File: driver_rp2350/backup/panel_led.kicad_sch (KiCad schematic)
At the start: 342 parts

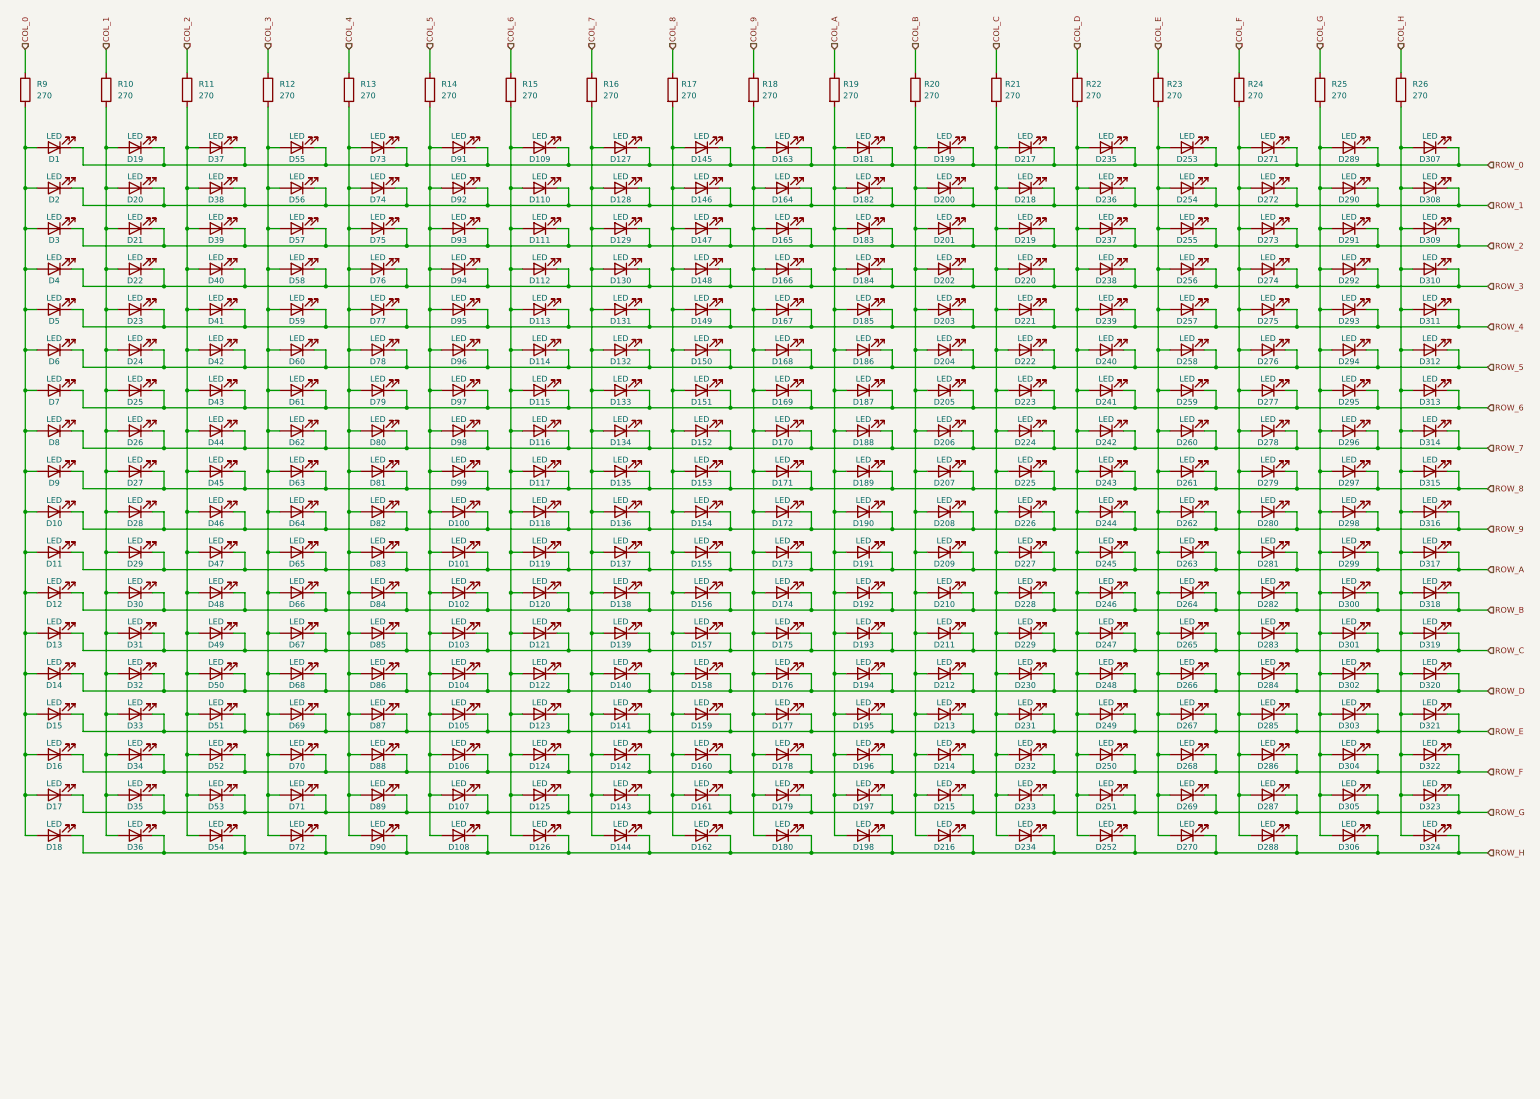
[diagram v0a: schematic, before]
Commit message: Renamed LED array due to kicad compatibility issues.
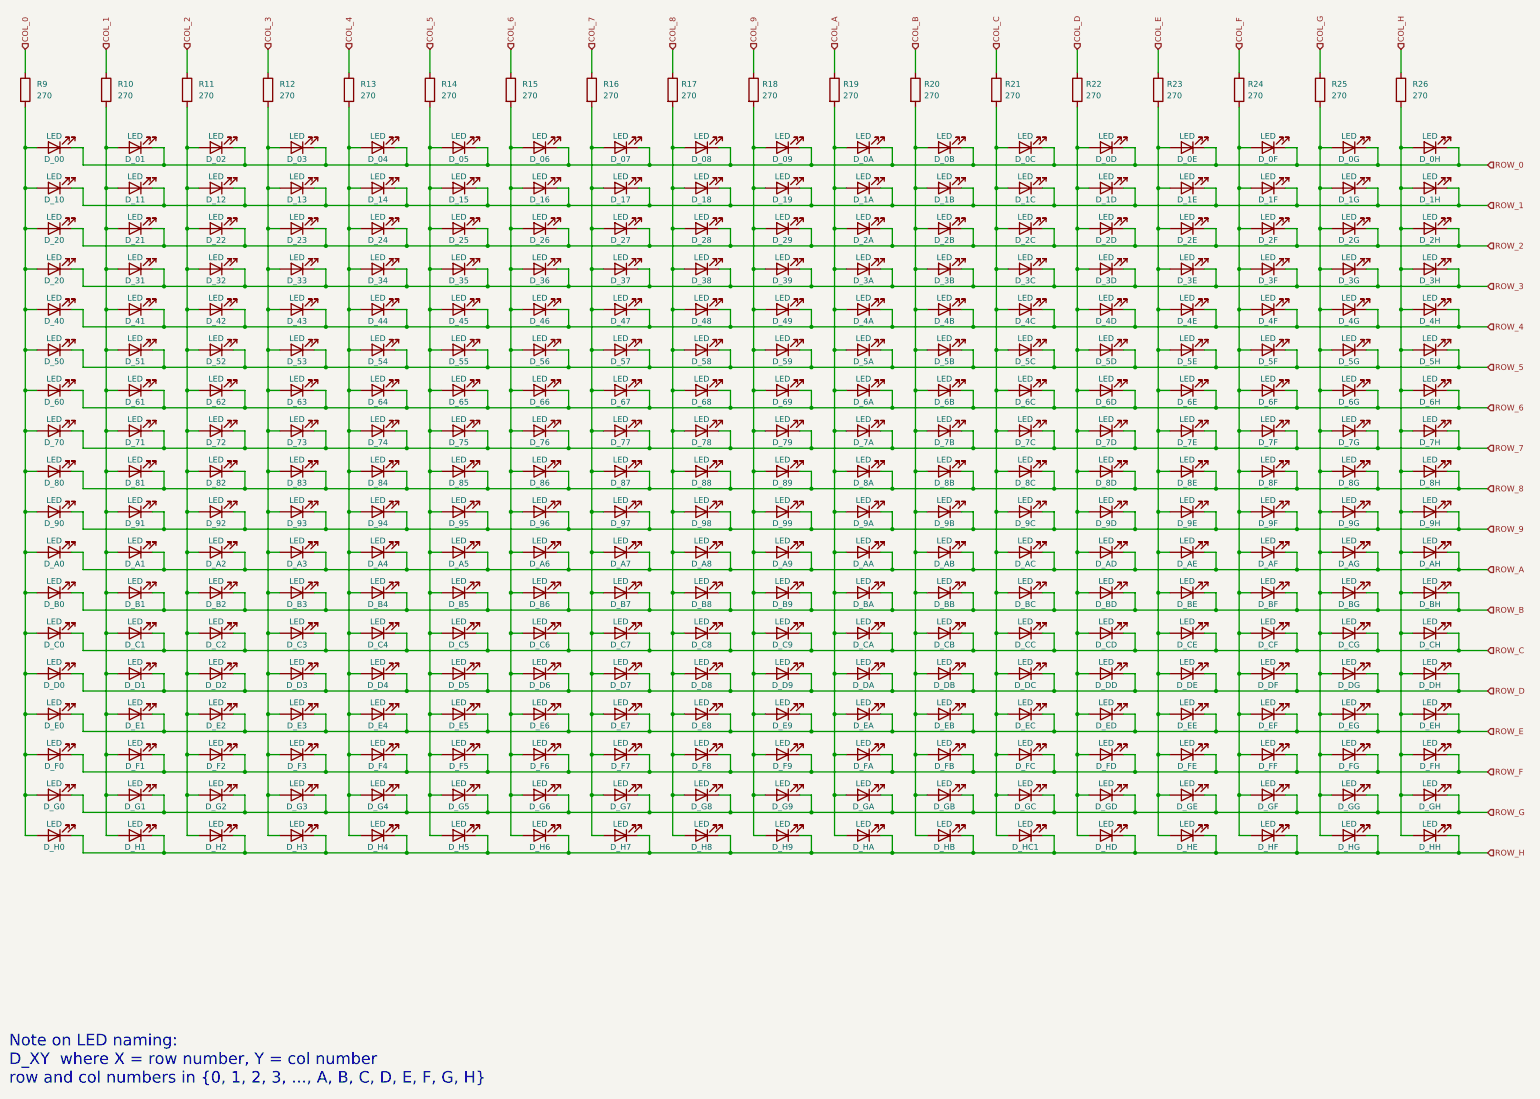
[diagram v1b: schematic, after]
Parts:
- removed D100, D101, D102, D103, D104, D105, D106, D107, D108, D109, D110, D111, D112, D113, D114, D115, D116, D117, D118, D119, D120, D121, D122, D123, D124, D125, D126, D127, D128, D129, D130, D131, D132, D133, D134, D135, D136, D137, D138, D139, D140, D141, D142, D143, D144, D145, D146, D147, D148, D149, D150, D151, D152, D153, D154, D155, D156, D157, D158, D159, D160, D161, D162, D163, D164, D165, D166, D167, D168, D169, D170, D171, D172, D173, D174, D175, D176, D177, D178, D179, D180, D181, D182, D183, D184, D185, D186, D187, D188, D189, D19, D190, D191, D192, D193, D194, D195, D196, D197, D198, D199, D20, D200, D201, D202, D203, D204, D205, D206, D207, D208, D209, D21, D210, D211, D212, D213, D214, D215, D216, D217, D218, D219, D22, D220, D221, D222, D223, D224, D225, D226, D227, D228, D229, D23, D230, D231, D232, D233, D234, D235, D236, D237, D238, D239, D24, D240, D241, D242, D243, D244, D245, D246, D247, D248, D249, D25, D250, D251, D252, D253, D254, D255, D256, D257, D258, D259, D26, D260, D261, D262, D263, D264, D265, D266, D267, D268, D269, D27, D270, D271, D272, D273, D274, D275, D276, D277, D278, D279, D28, D280, D281, D282, D283, D284, D285, D286, D287, D288, D289, D29, D290, D291, D292, D293, D294, D295, D296, D297, D298, D299, D30, D300, D301, D302, D303, D304, D305, D306, D307, D308, D309, D31, D310, D311, D312, D313, D314, D315, D316, D317, D318, D319, D32, D320, D321, D322, D323, D324, D33, D34, D35, D36, D37, D38, D39, D40, D41, D42, D43, D44, D45, D46, D47, D48, D49, D50, D51, D52, D53, D54, D55, D56, D57, D58, D59, D60, D61, D62, D63, D64, D65, D66, D67, D68, D69, D70, D71, D72, D73, D74, D75, D76, D77, D78, D79, D80, D81, D82, D83, D84, D85, D86, D87, D88, D89, D90, D91, D92, D93, D94, D95, D96, D97, D98, D99: LED, panel_custom:LED_0402_1005Metric, symbol Device:LED
- added D_01, D_02, D_03, D_04, D_05, D_06, D_07, D_08, D_09, D_0A, D_0B, D_0C, D_0D, D_0E, D_0F, D_0G, D_0H, D_11, D_12, D_13, D_14, D_15, D_16, D_17, D_18, D_19, D_1A, D_1B, D_1C, D_1D, D_1E, D_1F, D_1G, D_1H, D_21, D_22, D_23, D_24, D_25, D_26, D_27, D_28, D_29, D_2A, D_2B, D_2C, D_2D, D_2E, D_2F, D_2G, D_2H, D_31, D_32, D_33, D_34, D_35, D_36, D_37, D_38, D_39, D_3A, D_3B, D_3C, D_3D, D_3E, D_3F, D_3G, D_3H, D_41, D_42, D_43, D_44, D_45, D_46, D_47, D_48, D_49, D_4A, D_4B, D_4C, D_4D, D_4E, D_4F, D_4G, D_4H, D_51, D_52, D_53, D_54, D_55, D_56, D_57, D_58, D_59, D_5A, D_5B, D_5C, D_5D, D_5E, D_5F, D_5G, D_5H, D_61, D_62, D_63, D_64, D_65, D_66, D_67, D_68, D_69, D_6A, D_6B, D_6C, D_6D, D_6E, D_6F, D_6G, D_6H, D_71, D_72, D_73, D_74, D_75, D_76, D_77, D_78, D_79, D_7A, D_7B, D_7C, D_7D, D_7E, D_7F, D_7G, D_7H, D_81, D_82, D_83, D_84, D_85, D_86, D_87, D_88, D_89, D_8A, D_8B, D_8C, D_8D, D_8E, D_8F, D_8G, D_8H, D_91, D_92, D_93, D_94, D_95, D_96, D_97, D_98, D_99, D_9A, D_9B, D_9C, D_9D, D_9E, D_9F, D_9G, D_9H, D_A1, D_A2, D_A3, D_A4, D_A5, D_A6, D_A7, D_A8, D_A9, D_AA, D_AB, D_AC, D_AD, D_AE, D_AF, D_AG, D_AH, D_B1, D_B2, D_B3, D_B4, D_B5, D_B6, D_B7, D_B8, D_B9, D_BA, D_BB, D_BC, D_BD, D_BE, D_BF, D_BG, D_BH, D_C1, D_C2, D_C3, D_C4, D_C5, D_C6, D_C7, D_C8, D_C9, D_CA, D_CB, D_CC, D_CD, D_CE, D_CF, D_CG, D_CH, D_D1, D_D2, D_D3, D_D4, D_D5, D_D6, D_D7, D_D8, D_D9, D_DA, D_DB, D_DC, D_DD, D_DE, D_DF, D_DG, D_DH, D_E1, D_E2, D_E3, D_E4, D_E5, D_E6, D_E7, D_E8, D_E9, D_EA, D_EB, D_EC, D_ED, D_EE, D_EF, D_EG, D_EH, D_F1, D_F2, D_F3, D_F4, D_F5, D_F6, D_F7, D_F8, D_F9, D_FA, D_FB, D_FC, D_FD, D_FE, D_FF, D_FG, D_FH, D_G1, D_G2, D_G3, D_G4, D_G5, D_G6, D_G7, D_G8, D_G9, D_GA, D_GB, D_GC, D_GD, D_GE, D_GF, D_GG, D_GH, D_H1, D_H2, D_H3, D_H4, D_H5, D_H6, D_H7, D_H8, D_H9, D_HA, D_HB, D_HC1, D_HD, D_HE, D_HF, D_HG, D_HH: LED, panel_custom:LED_0402_1005Metric, symbol Device:LED
- renumbered D1 to D_00, D2 to D_10, D4 to D_20, D3 to D_20, D5 to D_40, D6 to D_50, D7 to D_60, D8 to D_70, D9 to D_80, D10 to D_90, D11 to D_A0, D12 to D_B0, D13 to D_C0, D14 to D_D0, D15 to D_E0, D16 to D_F0, D17 to D_G0, D18 to D_H0
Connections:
- net ROW_0: now also D_01.1 (K), D_02.1 (K), D_03.1 (K), D_04.1 (K), D_05.1 (K), D_06.1 (K), D_07.1 (K), D_08.1 (K), D_09.1 (K), D_0A.1 (K), D_0B.1 (K), D_0C.1 (K), D_0D.1 (K), D_0E.1 (K), D_0F.1 (K), D_0G.1 (K), D_0H.1 (K)
- net ROW_1: now also D_11.1 (K), D_12.1 (K), D_13.1 (K), D_14.1 (K), D_15.1 (K), D_16.1 (K), D_17.1 (K), D_18.1 (K), D_19.1 (K), D_1A.1 (K), D_1B.1 (K), D_1C.1 (K), D_1D.1 (K), D_1E.1 (K), D_1F.1 (K), D_1G.1 (K), D_1H.1 (K)
- net ROW_2: now also D_21.1 (K), D_22.1 (K), D_23.1 (K), D_24.1 (K), D_25.1 (K), D_26.1 (K), D_27.1 (K), D_28.1 (K), D_29.1 (K), D_2A.1 (K), D_2B.1 (K), D_2C.1 (K), D_2D.1 (K), D_2E.1 (K), D_2F.1 (K), D_2G.1 (K), D_2H.1 (K)
- net ROW_3: now also D_31.1 (K), D_32.1 (K), D_33.1 (K), D_34.1 (K), D_35.1 (K), D_36.1 (K), D_37.1 (K), D_38.1 (K), D_39.1 (K), D_3A.1 (K), D_3B.1 (K), D_3C.1 (K), D_3D.1 (K), D_3E.1 (K), D_3F.1 (K), D_3G.1 (K), D_3H.1 (K)
- net ROW_4: now also D_41.1 (K), D_42.1 (K), D_43.1 (K), D_44.1 (K), D_45.1 (K), D_46.1 (K), D_47.1 (K), D_48.1 (K), D_49.1 (K), D_4A.1 (K), D_4B.1 (K), D_4C.1 (K), D_4D.1 (K), D_4E.1 (K), D_4F.1 (K), D_4G.1 (K), D_4H.1 (K)
- net ROW_5: now also D_51.1 (K), D_52.1 (K), D_53.1 (K), D_54.1 (K), D_55.1 (K), D_56.1 (K), D_57.1 (K), D_58.1 (K), D_59.1 (K), D_5A.1 (K), D_5B.1 (K), D_5C.1 (K), D_5D.1 (K), D_5E.1 (K), D_5F.1 (K), D_5G.1 (K), D_5H.1 (K)
- net ROW_6: now also D_61.1 (K), D_62.1 (K), D_63.1 (K), D_64.1 (K), D_65.1 (K), D_66.1 (K), D_67.1 (K), D_68.1 (K), D_69.1 (K), D_6A.1 (K), D_6B.1 (K), D_6C.1 (K), D_6D.1 (K), D_6E.1 (K), D_6F.1 (K), D_6G.1 (K), D_6H.1 (K)
- net ROW_7: now also D_71.1 (K), D_72.1 (K), D_73.1 (K), D_74.1 (K), D_75.1 (K), D_76.1 (K), D_77.1 (K), D_78.1 (K), D_79.1 (K), D_7A.1 (K), D_7B.1 (K), D_7C.1 (K), D_7D.1 (K), D_7E.1 (K), D_7F.1 (K), D_7G.1 (K), D_7H.1 (K)
- net ROW_8: now also D_81.1 (K), D_82.1 (K), D_83.1 (K), D_84.1 (K), D_85.1 (K), D_86.1 (K), D_87.1 (K), D_88.1 (K), D_89.1 (K), D_8A.1 (K), D_8B.1 (K), D_8C.1 (K), D_8D.1 (K), D_8E.1 (K), D_8F.1 (K), D_8G.1 (K), D_8H.1 (K)
- net ROW_9: now also D_91.1 (K), D_92.1 (K), D_93.1 (K), D_94.1 (K), D_95.1 (K), D_96.1 (K), D_97.1 (K), D_98.1 (K), D_99.1 (K), D_9A.1 (K), D_9B.1 (K), D_9C.1 (K), D_9D.1 (K), D_9E.1 (K), D_9F.1 (K), D_9G.1 (K), D_9H.1 (K)
- net ROW_A: now also D_A1.1 (K), D_A2.1 (K), D_A3.1 (K), D_A4.1 (K), D_A5.1 (K), D_A6.1 (K), D_A7.1 (K), D_A8.1 (K), D_A9.1 (K), D_AA.1 (K), D_AB.1 (K), D_AC.1 (K), D_AD.1 (K), D_AE.1 (K), D_AF.1 (K), D_AG.1 (K), D_AH.1 (K)
- net ROW_B: now also D_B1.1 (K), D_B2.1 (K), D_B3.1 (K), D_B4.1 (K), D_B5.1 (K), D_B6.1 (K), D_B7.1 (K), D_B8.1 (K), D_B9.1 (K), D_BA.1 (K), D_BB.1 (K), D_BC.1 (K), D_BD.1 (K), D_BE.1 (K), D_BF.1 (K), D_BG.1 (K), D_BH.1 (K)
- net ROW_C: now also D_C1.1 (K), D_C2.1 (K), D_C3.1 (K), D_C4.1 (K), D_C5.1 (K), D_C6.1 (K), D_C7.1 (K), D_C8.1 (K), D_C9.1 (K), D_CA.1 (K), D_CB.1 (K), D_CC.1 (K), D_CD.1 (K), D_CE.1 (K), D_CF.1 (K), D_CG.1 (K), D_CH.1 (K)
- net ROW_D: now also D_D1.1 (K), D_D2.1 (K), D_D3.1 (K), D_D4.1 (K), D_D5.1 (K), D_D6.1 (K), D_D7.1 (K), D_D8.1 (K), D_D9.1 (K), D_DA.1 (K), D_DB.1 (K), D_DC.1 (K), D_DD.1 (K), D_DE.1 (K), D_DF.1 (K), D_DG.1 (K), D_DH.1 (K)
- net ROW_E: now also D_E1.1 (K), D_E2.1 (K), D_E3.1 (K), D_E4.1 (K), D_E5.1 (K), D_E6.1 (K), D_E7.1 (K), D_E8.1 (K), D_E9.1 (K), D_EA.1 (K), D_EB.1 (K), D_EC.1 (K), D_ED.1 (K), D_EE.1 (K), D_EF.1 (K), D_EG.1 (K), D_EH.1 (K)
- net ROW_F: now also D_F1.1 (K), D_F2.1 (K), D_F3.1 (K), D_F4.1 (K), D_F5.1 (K), D_F6.1 (K), D_F7.1 (K), D_F8.1 (K), D_F9.1 (K), D_FA.1 (K), D_FB.1 (K), D_FC.1 (K), D_FD.1 (K), D_FE.1 (K), D_FF.1 (K), D_FG.1 (K), D_FH.1 (K)
- net ROW_G: now also D_G1.1 (K), D_G2.1 (K), D_G3.1 (K), D_G4.1 (K), D_G5.1 (K), D_G6.1 (K), D_G7.1 (K), D_G8.1 (K), D_G9.1 (K), D_GA.1 (K), D_GB.1 (K), D_GC.1 (K), D_GD.1 (K), D_GE.1 (K), D_GF.1 (K), D_GG.1 (K), D_GH.1 (K)
- net ROW_H: now also D_H1.1 (K), D_H2.1 (K), D_H3.1 (K), D_H4.1 (K), D_H5.1 (K), D_H6.1 (K), D_H7.1 (K), D_H8.1 (K), D_H9.1 (K), D_HA.1 (K), D_HB.1 (K), D_HC1.1 (K), D_HD.1 (K), D_HE.1 (K), D_HF.1 (K), D_HG.1 (K), D_HH.1 (K)
- net at R17.2: now also D_08.2 (A), D_18.2 (A), D_28.2 (A), D_38.2 (A), D_48.2 (A), D_58.2 (A), D_68.2 (A), D_78.2 (A), D_88.2 (A), D_98.2 (A), D_A8.2 (A), D_B8.2 (A), D_C8.2 (A), D_D8.2 (A), D_E8.2 (A), D_F8.2 (A), D_G8.2 (A), D_H8.2 (A)
- net at R12.2: now also D_03.2 (A), D_13.2 (A), D_23.2 (A), D_33.2 (A), D_43.2 (A), D_53.2 (A), D_63.2 (A), D_73.2 (A), D_83.2 (A), D_93.2 (A), D_A3.2 (A), D_B3.2 (A), D_C3.2 (A), D_D3.2 (A), D_E3.2 (A), D_F3.2 (A), D_G3.2 (A), D_H3.2 (A)
- net at R24.2: now also D_0F.2 (A), D_1F.2 (A), D_2F.2 (A), D_3F.2 (A), D_4F.2 (A), D_5F.2 (A), D_6F.2 (A), D_7F.2 (A), D_8F.2 (A), D_9F.2 (A), D_AF.2 (A), D_BF.2 (A), D_CF.2 (A), D_DF.2 (A), D_EF.2 (A), D_FF.2 (A), D_GF.2 (A), D_HF.2 (A)
- net at R25.2: now also D_0G.2 (A), D_1G.2 (A), D_2G.2 (A), D_3G.2 (A), D_4G.2 (A), D_5G.2 (A), D_6G.2 (A), D_7G.2 (A), D_8G.2 (A), D_9G.2 (A), D_AG.2 (A), D_BG.2 (A), D_CG.2 (A), D_DG.2 (A), D_EG.2 (A), D_FG.2 (A), D_GG.2 (A), D_HG.2 (A)
- net at R21.2: now also D_0C.2 (A), D_1C.2 (A), D_2C.2 (A), D_3C.2 (A), D_4C.2 (A), D_5C.2 (A), D_6C.2 (A), D_7C.2 (A), D_8C.2 (A), D_9C.2 (A), D_AC.2 (A), D_BC.2 (A), D_CC.2 (A), D_DC.2 (A), D_EC.2 (A), D_FC.2 (A), D_GC.2 (A), D_HC1.2 (A)
- net at R13.2: now also D_04.2 (A), D_14.2 (A), D_24.2 (A), D_34.2 (A), D_44.2 (A), D_54.2 (A), D_64.2 (A), D_74.2 (A), D_84.2 (A), D_94.2 (A), D_A4.2 (A), D_B4.2 (A), D_C4.2 (A), D_D4.2 (A), D_E4.2 (A), D_F4.2 (A), D_G4.2 (A), D_H4.2 (A)
- net at R20.2: now also D_0B.2 (A), D_1B.2 (A), D_2B.2 (A), D_3B.2 (A), D_4B.2 (A), D_5B.2 (A), D_6B.2 (A), D_7B.2 (A), D_8B.2 (A), D_9B.2 (A), D_AB.2 (A), D_BB.2 (A), D_CB.2 (A), D_DB.2 (A), D_EB.2 (A), D_FB.2 (A), D_GB.2 (A), D_HB.2 (A)
- net at R26.2: now also D_0H.2 (A), D_1H.2 (A), D_2H.2 (A), D_3H.2 (A), D_4H.2 (A), D_5H.2 (A), D_6H.2 (A), D_7H.2 (A), D_8H.2 (A), D_9H.2 (A), D_AH.2 (A), D_BH.2 (A), D_CH.2 (A), D_DH.2 (A), D_EH.2 (A), D_FH.2 (A), D_GH.2 (A), D_HH.2 (A)
- net at R10.2: now also D_01.2 (A), D_11.2 (A), D_21.2 (A), D_31.2 (A), D_41.2 (A), D_51.2 (A), D_61.2 (A), D_71.2 (A), D_81.2 (A), D_91.2 (A), D_A1.2 (A), D_B1.2 (A), D_C1.2 (A), D_D1.2 (A), D_E1.2 (A), D_F1.2 (A), D_G1.2 (A), D_H1.2 (A)
- net at R23.2: now also D_0E.2 (A), D_1E.2 (A), D_2E.2 (A), D_3E.2 (A), D_4E.2 (A), D_5E.2 (A), D_6E.2 (A), D_7E.2 (A), D_8E.2 (A), D_9E.2 (A), D_AE.2 (A), D_BE.2 (A), D_CE.2 (A), D_DE.2 (A), D_EE.2 (A), D_FE.2 (A), D_GE.2 (A), D_HE.2 (A)
- net at R11.2: now also D_02.2 (A), D_12.2 (A), D_22.2 (A), D_32.2 (A), D_42.2 (A), D_52.2 (A), D_62.2 (A), D_72.2 (A), D_82.2 (A), D_92.2 (A), D_A2.2 (A), D_B2.2 (A), D_C2.2 (A), D_D2.2 (A), D_E2.2 (A), D_F2.2 (A), D_G2.2 (A), D_H2.2 (A)
- net at R14.2: now also D_05.2 (A), D_15.2 (A), D_25.2 (A), D_35.2 (A), D_45.2 (A), D_55.2 (A), D_65.2 (A), D_75.2 (A), D_85.2 (A), D_95.2 (A), D_A5.2 (A), D_B5.2 (A), D_C5.2 (A), D_D5.2 (A), D_E5.2 (A), D_F5.2 (A), D_G5.2 (A), D_H5.2 (A)
- net at R16.2: now also D_07.2 (A), D_17.2 (A), D_27.2 (A), D_37.2 (A), D_47.2 (A), D_57.2 (A), D_67.2 (A), D_77.2 (A), D_87.2 (A), D_97.2 (A), D_A7.2 (A), D_B7.2 (A), D_C7.2 (A), D_D7.2 (A), D_E7.2 (A), D_F7.2 (A), D_G7.2 (A), D_H7.2 (A)
- net at R19.2: now also D_0A.2 (A), D_1A.2 (A), D_2A.2 (A), D_3A.2 (A), D_4A.2 (A), D_5A.2 (A), D_6A.2 (A), D_7A.2 (A), D_8A.2 (A), D_9A.2 (A), D_AA.2 (A), D_BA.2 (A), D_CA.2 (A), D_DA.2 (A), D_EA.2 (A), D_FA.2 (A), D_GA.2 (A), D_HA.2 (A)
- net at R15.2: now also D_06.2 (A), D_16.2 (A), D_26.2 (A), D_36.2 (A), D_46.2 (A), D_56.2 (A), D_66.2 (A), D_76.2 (A), D_86.2 (A), D_96.2 (A), D_A6.2 (A), D_B6.2 (A), D_C6.2 (A), D_D6.2 (A), D_E6.2 (A), D_F6.2 (A), D_G6.2 (A), D_H6.2 (A)
- net at R18.2: now also D_09.2 (A), D_19.2 (A), D_29.2 (A), D_39.2 (A), D_49.2 (A), D_59.2 (A), D_69.2 (A), D_79.2 (A), D_89.2 (A), D_99.2 (A), D_A9.2 (A), D_B9.2 (A), D_C9.2 (A), D_D9.2 (A), D_E9.2 (A), D_F9.2 (A), D_G9.2 (A), D_H9.2 (A)
- net at R22.2: now also D_0D.2 (A), D_1D.2 (A), D_2D.2 (A), D_3D.2 (A), D_4D.2 (A), D_5D.2 (A), D_6D.2 (A), D_7D.2 (A), D_8D.2 (A), D_9D.2 (A), D_AD.2 (A), D_BD.2 (A), D_CD.2 (A), D_DD.2 (A), D_ED.2 (A), D_FD.2 (A), D_GD.2 (A), D_HD.2 (A)
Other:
- note added: "Note on LED naming: D_XY where X = row number, Y = col number row and col numbers in {0, 1, 2, 3, ..., A, B, C, D, E, F, G, H}"
